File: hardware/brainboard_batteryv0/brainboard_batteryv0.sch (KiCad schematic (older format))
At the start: 53 parts, among them CON1 USB-MINI-B, P1 JST, P2 PMIC, P3 TST, SW1 BAT_CHECK, SW2 BAT_CHECK, U1 MAX17043, U2 BQ27510, U3 MCP73831T, U4 TPS73233, U5 24C256, U6 BEAGLEBONE_BLACK

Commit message: Reorganized sch a bit
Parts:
- removed D3: BATTGOOD, ~, symbol LED
- removed R11: 330, ~, symbol R
- removed SW2: BAT_CHECK, ~, symbol SW_PUSH
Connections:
- wire segments 189 -> 185
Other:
- note added: "TO DO:\n- Connection to BATT_LO/GD on P8\n- Jpr w/ above for /ALRT\n- Adj LDO to compensate for D4"
- moved on the sheet: C1, C10, C11, C12, C13, C2, C3, C4, C5, C6, C7, C8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

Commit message: More battery changes
Added power-down logic to battery board (currently faulty, need
revision); added fuel gauge, 2-pin JST, and BBB battery connector to
Brainboard R1.
TODO: Fix power-down logic (suggest dedicated power-button supervisor
like STM660x), add isolation so board can be safely plugged in to charge
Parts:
- removed C11: 4.7nF, ~, symbol C
- removed C3, C6, C8: 0.1uF, ~, symbol C
- removed C9: 0.47uF, ~, symbol C
- removed R1: 0.01, ~, symbol R
- removed R12: 2K, ~, symbol R
- removed R3: 1.8M, ~, symbol R
- removed R4: 18.2k, ~, symbol R
- removed R6: 100, ~, symbol R
- removed SW1: BAT_CHECK, ~, symbol SW_PUSH
- removed U2: BQ27510, symbol BQ27510
- removed U3: MCP73831T, symbol MCP73831T
- added P2: VBAT, ~, symbol TST
- added P3: GND, ~, symbol TST
- added P4: VBUS, ~, symbol TST
- added P6: ~ALRT, ~, symbol TST
- added P8: PREREG, ~, symbol TST
- added P9: 3V3, ~, symbol TST
- added R11: 5M, ~, symbol R
- added R13: 1k, ~, symbol R
- added S1: SYSOFF, ~, symbol SMT_BUTTON
- added S2: BBB_POWER, ~, symbol SMT_BUTTON
- added SJ1, SJ2: BAT, SparkFun-Passives-SJ_2S-NO, symbol SOLDERJUMPERNO
- added SJ5: AUTO_SYSOFF, SparkFun-Passives-SJ_2S-NO, symbol SOLDERJUMPERNO
- added SJ6: SYSOFF_DIS, SparkFun-Passives-SJ_2S-NO, symbol SOLDERJUMPERNO
- added U2: BQ24075(T), symbol BQ24075(T)
- added U4: SN74LVC2G132, symbol SN74LVC2G132
- added U5: MC74VHC1G03, ~, symbol MC74VHC1G03
- C3: renamed from C10; value 4.7nF -> 1uF
- C4: value 0.1uF -> 1uF
- C5: value 0.1uF -> 4.7uF
- C7: value 33nF -> 1uF
- D1: value BATTGOOD -> PGOOD
- P5: renamed from P2; value PMIC -> BBB_PMIC
- P7: renamed from P3; value TST -> WP
- R10: value 330 -> 1k
- R14: value 2M -> 100k
- R15: value 430K -> 100k
- R7: value 100 -> 3k
- R8: value 1k -> 5M
- R9: value 330 -> 2.4k
- U1: value MAX17043 -> MAX17043/8
- renumbered C12 to C6, C13 to C8, D4 to D3, R2 to R1, R19 to R12, R20 to R16, R21 to R17, R18 to R2, R5 to R3, R13 to R4, R16 to R5, R17 to R6, SJ1 to SJ3, SJ2 to SJ4, U5 to U3, U4 to U6, U6 to U7
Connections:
- net labels added: BBB_TS, EN1, EN2, ILIM, ISET, OUT, PWR_BUT, SYSOFF, SYSOFF_BUT, SYS_5V, ~ALRT, ~CHG, ~PGOOD
- net labels removed: -BATT, /ALRT, BI/TOUT, EN, PROG, REG25, SRN, SRP, STAT, TS, VCC
- wire segments 185 -> 215
- no-connect marks 81 -> 80
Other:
- note added: "Battery charger"
- note added: "BeagleBone Black battery connector included \nfor experimentation; DO NOT COMBINE with\non-board charger and LDO"
- note added: "Fast charging current = K_ISET/R_ISET\nK_ISET = [797..975], 890 typical\nR_ISET = 2.4k yields about 400mA, or 0.2C \nfor 2000mAh cell\n\nInput current limit = K_ILIM/R_ILIM\nSee datasheet for K_ILIM ranges\nR_ILIM = 3k yields 500mA"
- note added: "Power-off logic"
- note added: "TO DO:\n- Connection to ~ALRT~ on P8"
- note added: "The 3.3V rail generated on-board is used when\noperating independently of the BeagleBone Black.\nD3 prevents reverse current in the event\nthe BBB is accidentally used for power. Brainboard\ncircuits can all tolerate voltage drop across D3."
- note removed: "BeagleBone Black battery connector:\nIncluded for experimentation; if used,\nwould make charger and LDO unnecessary"
- note removed: "Maybe DNP in final version: this is just so we \nhave a fuel gauge if I can't figure out the bq27510"
- note removed: "TO DO:\n- Connection to BATT_LO/GD on P8\n- Jpr w/ above for /ALRT\n- Adj LDO to compensate for D4"
- note removed: "The 3.3V rail generated on-board is used when\noperating independently of the BeagleBone Black.\nSchottky prevents reverse current in the event\nthe BBB is accidentally used for power."
- note removed: "USB battery charging"
- note removed: "VBAT < 2.826 V will disable\nthe voltage regulator to\nminimize over-discharge.\n\nEN pin on TPS73233 turns\nregulator off at < 0.5 V."
- moved on the sheet: C1, C2, C6, C8, CON1, D2, D3, P1, P5, P7, R1, R12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

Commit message: Just gonna use separate button for SYSOFF
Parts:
- removed C7: 1uF, ~, symbol C
- removed R11: 5M, ~, symbol R
- removed R14, R15: 100k, ~, symbol R
- removed S1: SYSOFF, ~, symbol SMT_BUTTON
- removed SJ5: AUTO_SYSOFF, SparkFun-Passives-SJ_2S-NO, symbol SOLDERJUMPERNO
- removed SJ6: SYSOFF_DIS, SparkFun-Passives-SJ_2S-NO, symbol SOLDERJUMPERNO
- removed U4: SN74LVC2G132, symbol SN74LVC2G132
- removed U5: MC74VHC1G03, ~, symbol MC74VHC1G03
- removed U6: TPS73233, ~, symbol TPS73233
- added C11: 0.47uF, ~, symbol C
- added C5: 0.01uF, ~, symbol C
- added D1: PMEG1020EJ, ~, symbol DIODESCH
- added F?: PPTC 1A, ~, symbol FUSE
- added P10: SYSOFF, ~, symbol TST
- added R16: 1.2M, ~, symbol R
- added R17: 60.4k, ~, symbol R
- added R18: 29.4k, ~, symbol R
- added R7: 5M, ~, symbol R
- added S2: POWER, ~, symbol SMT_BUTTON
- added SJ5: SYSOFF_DIS, SparkFun-Passives-SJ_3_PASTE1&2, symbol SOLDERJUMPER_2WAYPASTE1&2
- added SJ6: TO PMIC, SparkFun-Passives-SJ_2S, symbol SOLDERJUMPERNC
- added U4: TPS73201, ~, symbol TPS732XX
- added U5: LTC2951-2, ~, symbol LTC2951-2
- C3: value 1uF -> 10uF
- C4: value 1uF -> 4.7uF
- D5: renamed from D3; value DIODESCH -> PMEG1020EJ
- R10: renamed from R9; value 2.4k -> 2.2k
- R11: renamed from R10; value 1k -> 1.5k
- R12: value 10K -> 10k
- R13: value 1k -> 1.5k
- R14: renamed from R16; value 5.6K -> 5.6k
- R15: renamed from R17; value 5.6K -> 5.6k
- R3: value 1K -> 1k
- R4, R5, R6: value 4.7K -> 4.7k
- R8: value 5M -> 1.2M
- R9: renamed from R7; value 3k -> 1.18k
- S1: renamed from S2; value BBB_POWER -> SYSOFF
- renumbered C8 to C10, C5 to C6, C6 to C9, D1 to D3, D2 to D4, P3 to P2, P2 to P3, P5 to P4, P4 to P5, U7 to U8
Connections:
- net labels added: FB, REGOUT
- net labels removed: 3V3_ONBOARD, NR, PWR_BUT, SYSOFF_BUT, SYS_5V
- wire segments 215 -> 210
- no-connect marks 80 -> 82
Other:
- note added: "Brief SYSOFF press latches EN low ("on").\nLong (3 sec) press latches EN hi-Z ("off")."
- note added: "C_OFFT = (1.56e-4 uF/ms)*(t_offt - 33 ms)\n\nC_OFFT = 0.47 uF --> t_offt = 3.045 s\n"
- note added: "Fast charging current = K_ISET/R_ISET\nK_ISET = [797..975], 890 typical\nR_ISET = 2.2k yields about 400mA, or 0.2C \nfor 2000mAh cell\n\nInput current limit = K_ILIM/R_ILIM\nSee datasheet for K_ILIM ranges\nR_ILIM = 1.18k yields 1.3A\n\nFloating TMR gives default fast-charge\nsafety cutoff of 5 hours"
- note added: "REGOUT = 1.204*(R17+R18)/R18"
- note added: "TO DO:\n- Connection to ~ALRT~ on P8\n- Hurr how do I overcurrent/voltage protection"
- note added: "The 3.3V rail generated on-board is used when\noperating independently of the BeagleBone Black.\nD5 prevents reverse current in the event\nthe BBB is accidentally used for power.\n\nREGOUT is adjusted to compensate for 365 mV\ndrop across D5."
- note added: "Undervoltage detection: disconnects battery if\nVBATT < 3.1 V"
- note removed: "Fast charging current = K_ISET/R_ISET\nK_ISET = [797..975], 890 typical\nR_ISET = 2.4k yields about 400mA, or 0.2C \nfor 2000mAh cell\n\nInput current limit = K_ILIM/R_ILIM\nSee datasheet for K_ILIM ranges\nR_ILIM = 3k yields 500mA"
- note removed: "TO DO:\n- Connection to ~ALRT~ on P8"
- note removed: "The 3.3V rail generated on-board is used when\noperating independently of the BeagleBone Black.\nD3 prevents reverse current in the event\nthe BBB is accidentally used for power. Brainboard\ncircuits can all tolerate voltage drop across D3."
- moved on the sheet: C1, C10, C2, C3, C9, D3, D4, D5, P1, P2, P3, P5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

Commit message: Semi-finished battery board rev0
Everything laid out and routed, still need to check alignment of BBB
battery connector holes
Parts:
- removed C1: 0.01uF, ~, symbol C
- removed D1: PMEG1020EJ, ~, symbol DIODESCH
- removed F?: PPTC 1A, ~, symbol FUSE
- removed R1: 180, ~, symbol R
- removed R3: 1k, ~, symbol R
- removed SJ5: SYSOFF_DIS, SparkFun-Passives-SJ_3_PASTE1&2, symbol SOLDERJUMPER_2WAYPASTE1&2
- removed U4: TPS73201, ~, symbol TPS732XX
- removed U5: LTC2951-2, ~, symbol LTC2951-2
- added C11: 0.1uF, ~, symbol C
- added C3, C4: 10uF, ~, symbol C
- added D1: SMAJ7.0A, ~, symbol ZENER
- added F1, F2: PTC 1.95A, ~, symbol FUSE
- added Q1: SI2312, ~, symbol MOS_N_E
- added R16: 52.3k, ~, symbol R
- added SJ6: LOWBAT_DIS, SparkFun-Passives-SJ_3_PASTE1&2, symbol SOLDERJUMPER_2WAYPASTE1&2
- added SJ7: SENSE, SparkFun-Passives-SJ_2S-NO, symbol SOLDERJUMPERNO
- added U4: TPS73601-SON, ~, symbol TPS736XX-SON
- added U5: LTC2951-1, ~, symbol LTC2951-1
- C1: renamed from C2; value 1uF -> 0.1uF
- C10: value 0.1uF -> 2.2uF
- C2: renamed from C4; value 4.7uF -> 10uF
- C7: renamed from C6; value 4.7uF -> 10uF
- D4: renamed from D5; value PMEG1020EJ -> PMEG2005AEA
- P8: renamed from P10; value SYSOFF -> EN
- R14: renamed from R18; value 29.4k -> 30.1k
- R15: renamed from R17; value 60.4k -> 52.3k
- R17: renamed from R16; value 1.2M -> 806k
- R5: renamed from R7; value 5M -> 806k
- R6: renamed from R8; value 1.2M -> 191k
- S2: value POWER -> BBB_SLEEP
- SJ3: renamed from SJ6; value TO PMIC -> TS PMIC
- U1: value MAX17043/8 -> MAX17048
- U2: value BQ24075(T) -> BQ24074(T)
- renumbered C3 to C5, C5 to C6, C9 to C8, C11 to C9, D3 to D2, D4 to D3, P9 to P10, P3 to P2, P2 to P3, P6 to P5, P5 to P6, P8 to P9, R2 to R1, R11 to R10, R13 to R11, R14 to R12, R15 to R13, R4 to R2, R5 to R3, R6 to R4, R9 to R7, R10 to R8, R12 to R9, SJ3 to SJ4, SJ4 to SJ5, U8 to U6
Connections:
- net labels added: B+, B-, EN, LOWBAT, OFFT, PWR_BUT, TMR, TS, VIN, ~KILL, ~PB
- net labels removed: EN2, SYSOFF
- wire segments 210 -> 242
- no-connect marks 82 -> 81
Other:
- note added: "Brief SYSOFF press latches EN hi-Z ("on").\nLong (3 sec) press latches EN low ("off")."
- note added: "DNP"
- note added: "Fast charging current = K_ISET/R_ISET\nK_ISET = [797..975], 890 typical\nR_ISET = 2.2k yields about 400mA, or 0.2C \nfor 2000mAh cell\n\nInput current limit = K_ILIM/R_ILIM\nSee datasheet for K_ILIM ranges\nR_ILIM = 1.18k yields 1.3A"
- note added: "Reverse\npolarity\nprotection"
- note added: "TO DO:\n- Connection to ~ALRT~ on P8"
- note added: "TPS73601 can supply up to\n400mA w/ VDO = 70 mV\n@ 25 deg C"
- note added: "T_MAXCHG = 10*K_TMR*R_TMR\nK_TMR = 48s/kOhm\nR_TMR = 52.3k gives about 7 hr safety cutoff"
- note added: "The 3.3V rail generated on-board is used when\noperating independently of the BeagleBone Black.\nD3 prevents reverse current in the event\nthe BBB is accidentally used for power.\n\nREGOUT can be adjusted to compensate for \nvoltage drop across D3, or D3 can be DNP and shorted."
- note added: "Undervoltage detection: ~KILL~ < 0.6V\nif VBATT < 3.1V, turning off regulator"
- note removed: "Brief SYSOFF press latches EN low ("on").\nLong (3 sec) press latches EN hi-Z ("off")."
- note removed: "Fast charging current = K_ISET/R_ISET\nK_ISET = [797..975], 890 typical\nR_ISET = 2.2k yields about 400mA, or 0.2C \nfor 2000mAh cell\n\nInput current limit = K_ILIM/R_ILIM\nSee datasheet for K_ILIM ranges\nR_ILIM = 1.18k yields 1.3A\n\nFloating TMR gives default fast-charge\nsafety cutoff of 5 hours"
- note removed: "TO DO:\n- Connection to ~ALRT~ on P8\n- Hurr how do I overcurrent/voltage protection"
- note removed: "The 3.3V rail generated on-board is used when\noperating independently of the BeagleBone Black.\nD5 prevents reverse current in the event\nthe BBB is accidentally used for power.\n\nREGOUT is adjusted to compensate for 365 mV\ndrop across D5."
- note removed: "Undervoltage detection: disconnects battery if\nVBATT < 3.1 V"
- moved on the sheet: C1, C10, C2, C5, C7, C8, D4, P1, P10, P2, P3, P5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

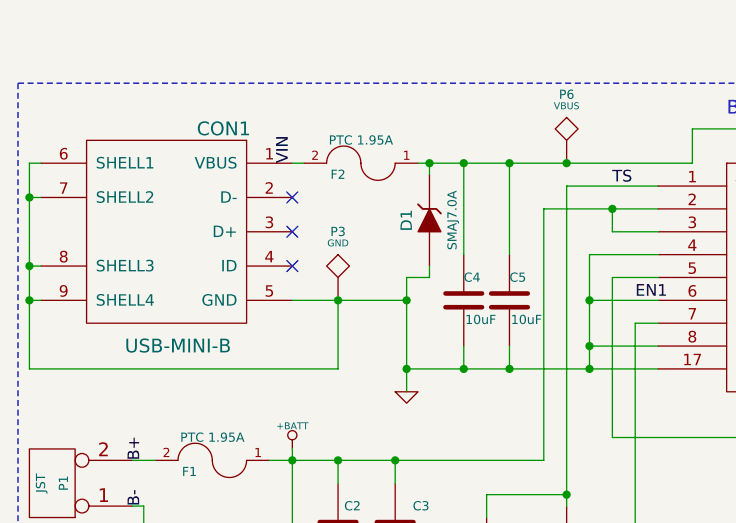
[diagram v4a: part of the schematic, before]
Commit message: Finalized hole positions, gerbers/drills
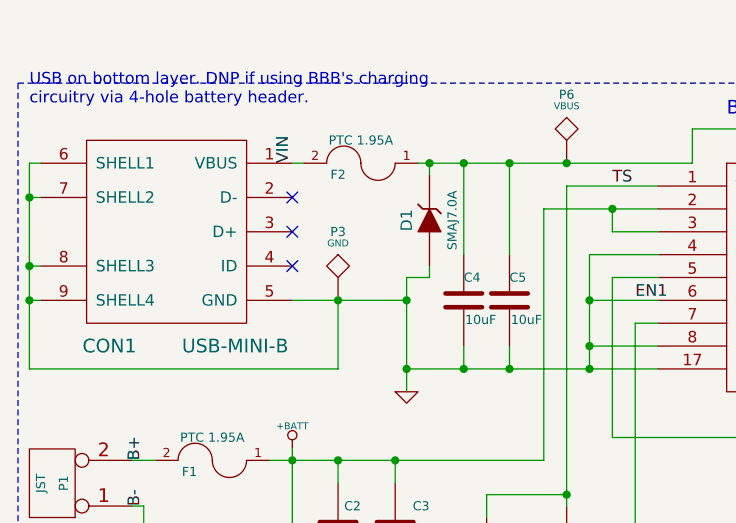
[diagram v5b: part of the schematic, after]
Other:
- note added: "USB on bottom layer. DNP if using BBB's charging\ncircuitry via 4-hole battery header."
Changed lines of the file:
@@
 Sheet 1 1
 Title ""
-Date "29 jan 2014"
+Date "30 jan 2014"
 Rev ""
 Comp ""
@@
 U 1 1 52C3190B
 P 1200 1200
-F 0 "CON1" H 950 1650 60  0000 C CNN
-F 1 "USB-MINI-B" H 1150 700 60  0000 C CNN
+F 0 "CON1" H 1450 700 60  0000 C CNN
+F 1 "USB-MINI-B" H 900 700 60  0000 C CNN
 F 2 "~" H 1200 1200 60  0000 C CNN
 F 3 "~" H 1200 1200 60  0000 C CNN
@@
 Wire Wire Line
 	1500 6100 1500 6500
+Text Notes 600  650  0    51   ~ 0
+USB on bottom layer. DNP if using BBB's charging\ncircuitry via 4-hole battery header.
 $EndSCHEMATC
